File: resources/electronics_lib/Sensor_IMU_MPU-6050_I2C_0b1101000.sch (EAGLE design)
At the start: 7 parts

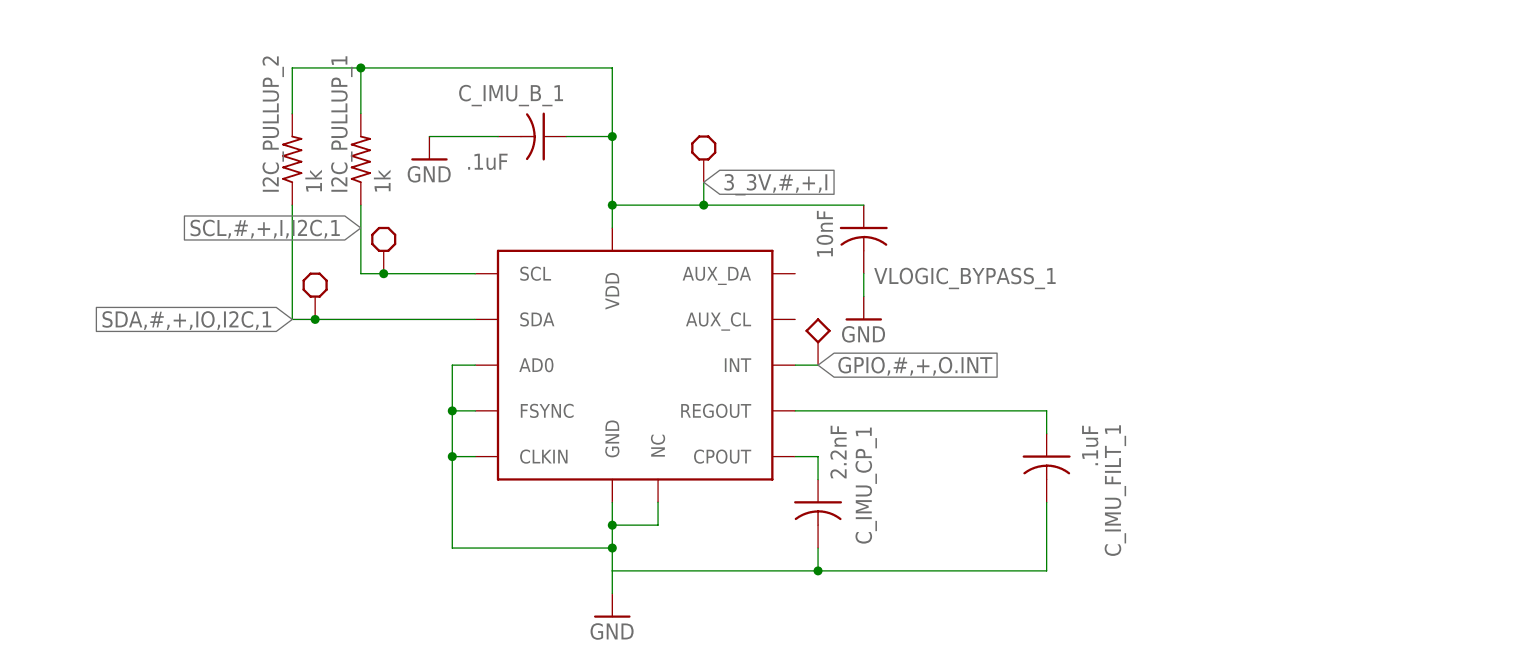
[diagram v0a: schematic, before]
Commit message: Updated electronics block library.
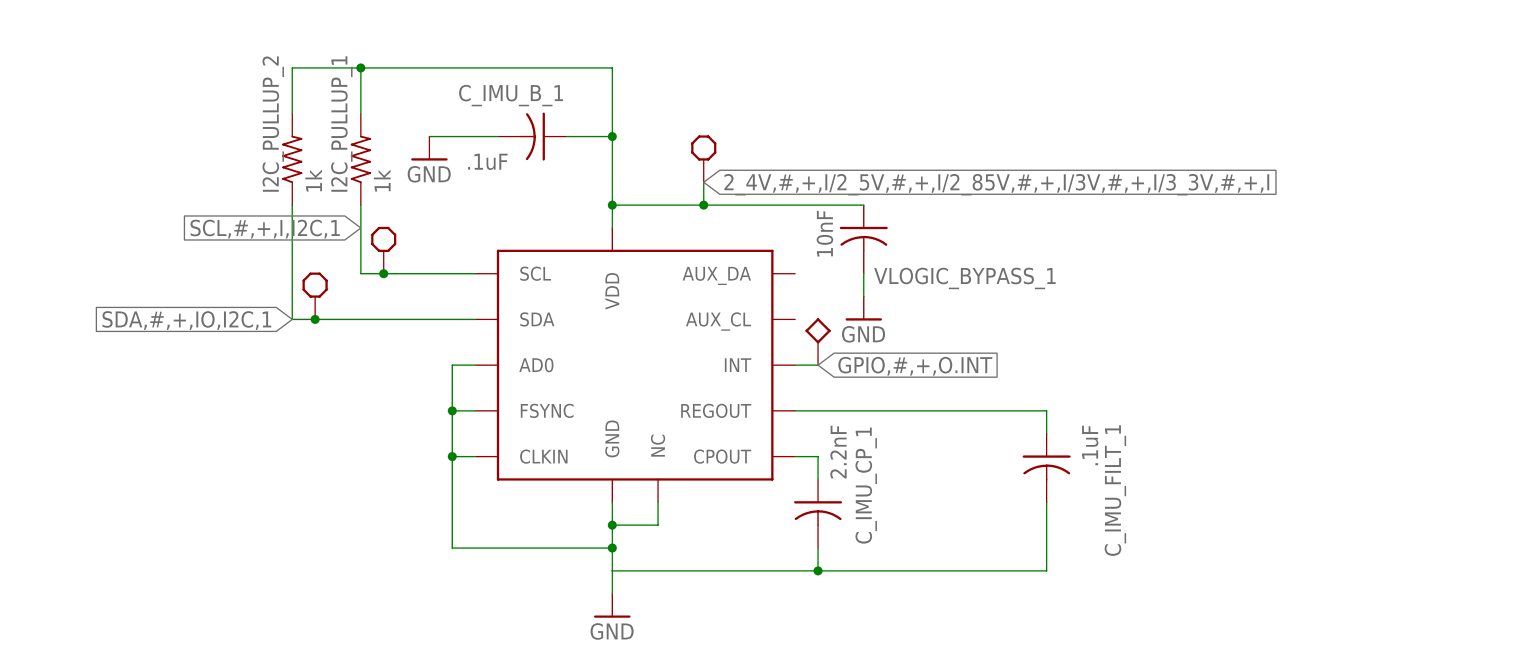
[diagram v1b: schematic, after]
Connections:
- net 3_3V,#,+,I renamed 2_4V,#,+,I/2_5V,#,+,I/2_85V,#,+,I/3V,#,+,I/3_3V,#,+,I
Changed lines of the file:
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@@
 <description>&lt;b&gt;Inertial Measurement Unit via I2C&lt;/b&gt;
 &lt;p&gt;&lt;a href="http://www.invensense.com/mems/gyro/documents/PS-MPU-6000A.pdf"&gt;MPU-6050&lt;/a&gt;&lt;/p&gt;
-&lt;p&gt;Connect IMU_SCL_x to the SCL pin on the microcontroller&lt;/p&gt;
-&lt;p&gt;Connect IMU_SDA_x to the SDA pin on the microcontroller&lt;/p&gt;
-&lt;p&gt;Connect IMU_IRQ_x to an interruptable pin on the microcontroller&lt;/p&gt;
-&lt;p&gt;This block includes all supply bypass capacitors.&lt;/p&gt;</description>
+&lt;p&gt;I2C address: 0b1101000&lt;/p&gt;</description>
 <plain>
 </plain>
@@
 </segment>
 </net>
-<net name="3_3V,#,+,I" class="0">
+<net name="2_4V,#,+,I/2_5V,#,+,I/2_85V,#,+,I/3V,#,+,I/3_3V,#,+,I" class="0">
 <segment>
 <pinref part="VLOGIC_BYPASS_1" gate="G$1" pin="1"/>
